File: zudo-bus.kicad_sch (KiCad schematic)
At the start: 56 parts, among them P1 WJ500V-5.08-2P-14-00A, P2 WJ500V-5.08-2P-14-00A, U10 2541WR-2X08P, U11 2541WR-2X08P, U12 1217754-1, U13 1217754-1, U14 1217754-1, U15 1217754-1, U2 2541WR-2X08P, U3 YLED0603YG, U4 NCD1608A1, U5 2541WR-2X08P, U6 2541WR-2X08P, U7 2541WR-2X08P, U8 2541WR-2X08P, U9 2541WR-2X08P

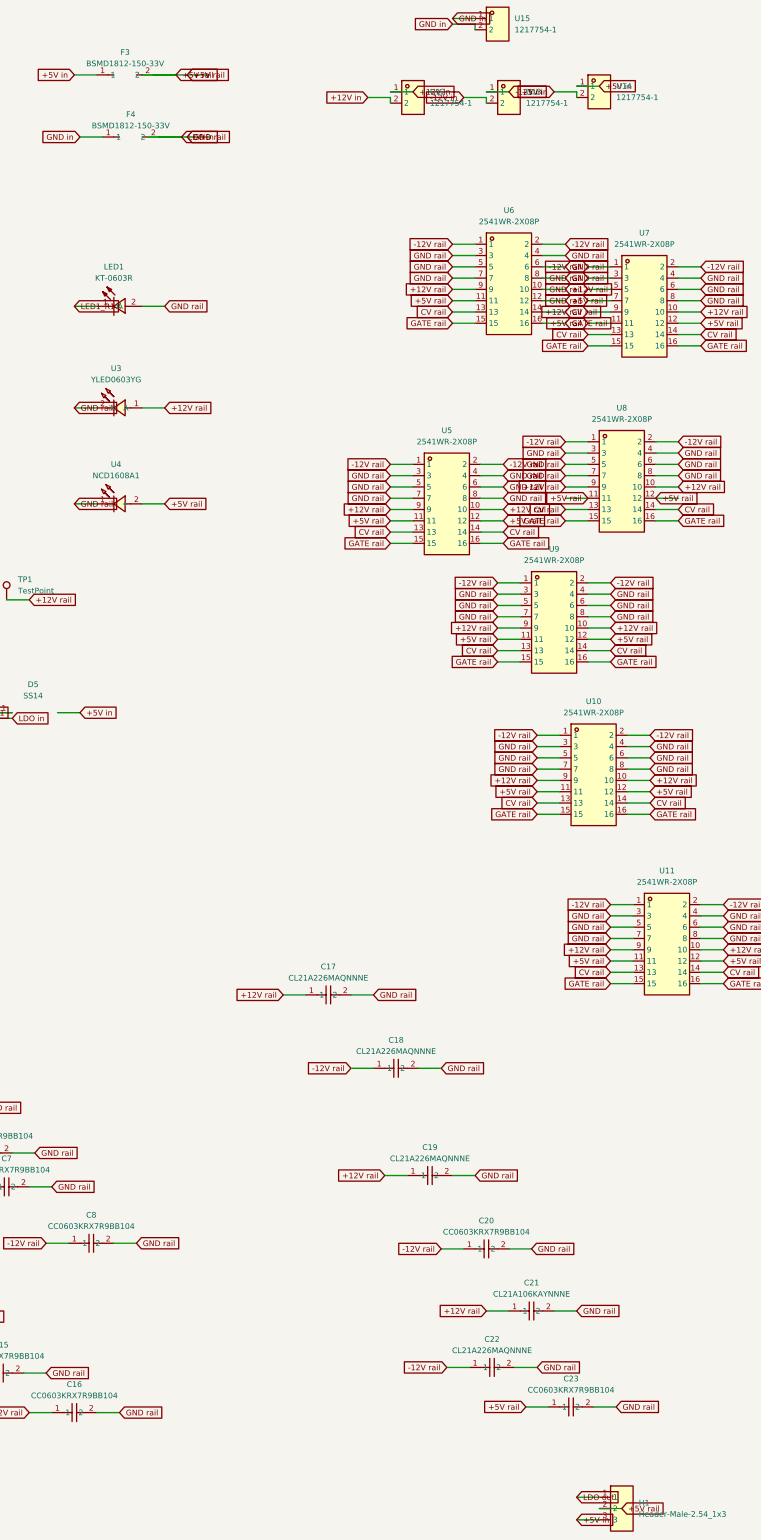
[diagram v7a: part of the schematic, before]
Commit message: Fix H1 label direction and remove duplicate FASTON labels
Corrections:
- H1: Revert +5V rail to point left (pins are on left side)
- Remove duplicate +12V in at (210.82, 35.56) - FASTON area
- Remove duplicate -12V in at (232.41, 35.56) - FASTON area
- Remove duplicate +5V in at (252.73, 34.29) - FASTON area
- Remove duplicate +5V in at (135.89, 175.26) - D5 area

Final label pattern:
- 2-pin horizontal components: left label ←, right label →
- FASTON (1-pin): label pointing ←
- H1 header (pins on left): all labels pointing ←

Co-Authored-By: Claude Opus 4.5 <noreply@anthropic.com>
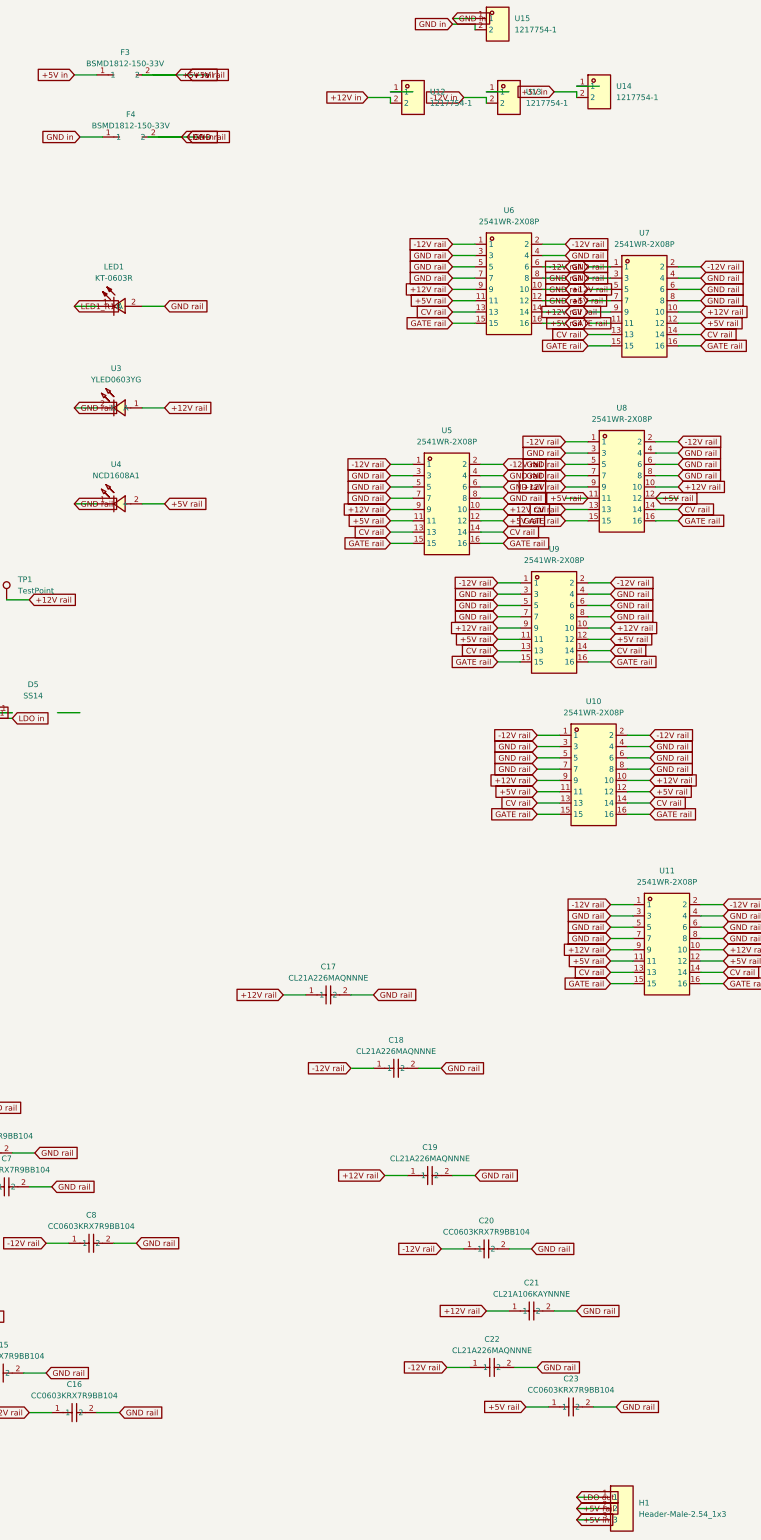
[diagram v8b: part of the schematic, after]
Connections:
- net +12V in: no longer U12.1
- net +5V in: no longer U13.1, U14.1
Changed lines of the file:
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@@
-		)
-	)
-	(global_label "+5V in"
-		(shape input)
-		(at 135.89000000000001 175.26 0)
-		(effects
-			(font
-				(size 1.27 1.27)
-			)
-			(justify left)
-		)
-		(uuid "p0000001-0001-0001-0001-000000000018")
-		(property "Intersheetrefs" "${INTERSHEET_REFS}"
-			(at 130.81 175.26 0)
-			(effects
-				(font
-					(size 1.27 1.27)
-				)
-				(hide yes)
-			)
 		)
 	)
@@
 		)
 	)
-	(global_label "+12V in"
-		(shape input)
-		(at 210.82000000000002 35.56 0)
-		(effects
-			(font
-				(size 1.27 1.27)
-			)
-			(justify left)
-		)
-		(uuid "p0000001-0001-0001-0001-000000000034")
-		(property "Intersheetrefs" "${INTERSHEET_REFS}"
-			(at 205.74 35.56 0)
-			(effects
-				(font
-					(size 1.27 1.27)
-				)
-				(hide yes)
-			)
-		)
-	)
-	(global_label "-12V in"
-		(shape input)
-		(at 232.41000000000003 35.56 0)
-		(effects
-			(font
-				(size 1.27 1.27)
-			)
-			(justify left)
-		)
-		(uuid "p0000001-0001-0001-0001-000000000035")
-		(property "Intersheetrefs" "${INTERSHEET_REFS}"
-			(at 227.33 35.56 0)
-			(effects
-				(font
-					(size 1.27 1.27)
-				)
-				(hide yes)
-			)
-		)
-	)
-	(global_label "+5V in"
-		(shape input)
-		(at 252.73000000000002 34.29 0)
-		(effects
-			(font
-				(size 1.27 1.27)
-			)
-			(justify left)
-		)
-		(uuid "p0000001-0001-0001-0001-000000000036")
-		(property "Intersheetrefs" "${INTERSHEET_REFS}"
-			(at 247.65 34.29 0)
-			(effects
-				(font
-					(size 1.27 1.27)
-				)
-				(hide yes)
-			)
-		)
-	)
 	(global_label "GND in"
 		(shape input)
@@
 	(global_label "+5V rail"
 		(shape input)
-		(at 257.81 354.33 0)
+		(at 247.65 354.33 180)
 		(effects
 			(font
@@
 	(wire
 		(pts
-			(xy 252.73 354.33) (xy 257.81 354.33)
-		)
-		(stroke
+			(xy 252.73 354.33) (xy 247.65 354.33)
+		)
+		(stroke
